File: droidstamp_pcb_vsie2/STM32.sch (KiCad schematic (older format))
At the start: 51 parts, among them P6 CONN_5X2, P8 CONN_12X2, P9 CONN_12X2, Q2 BS170F, Q3 BS170F, Q4 BS170F, Q5 BS170F, Q6 BS170F, Q7 BS170F, Q8 BS170F, Q9 BS170F, U10 STM32F105RC, U11 LT1117CST-3.3, U12 ZXMHC3F381N8, U13 ZXMHC3F381N8, U14 ZXMHC3F381N8, U15 ZXMHC3F381N8, X3 12MHz

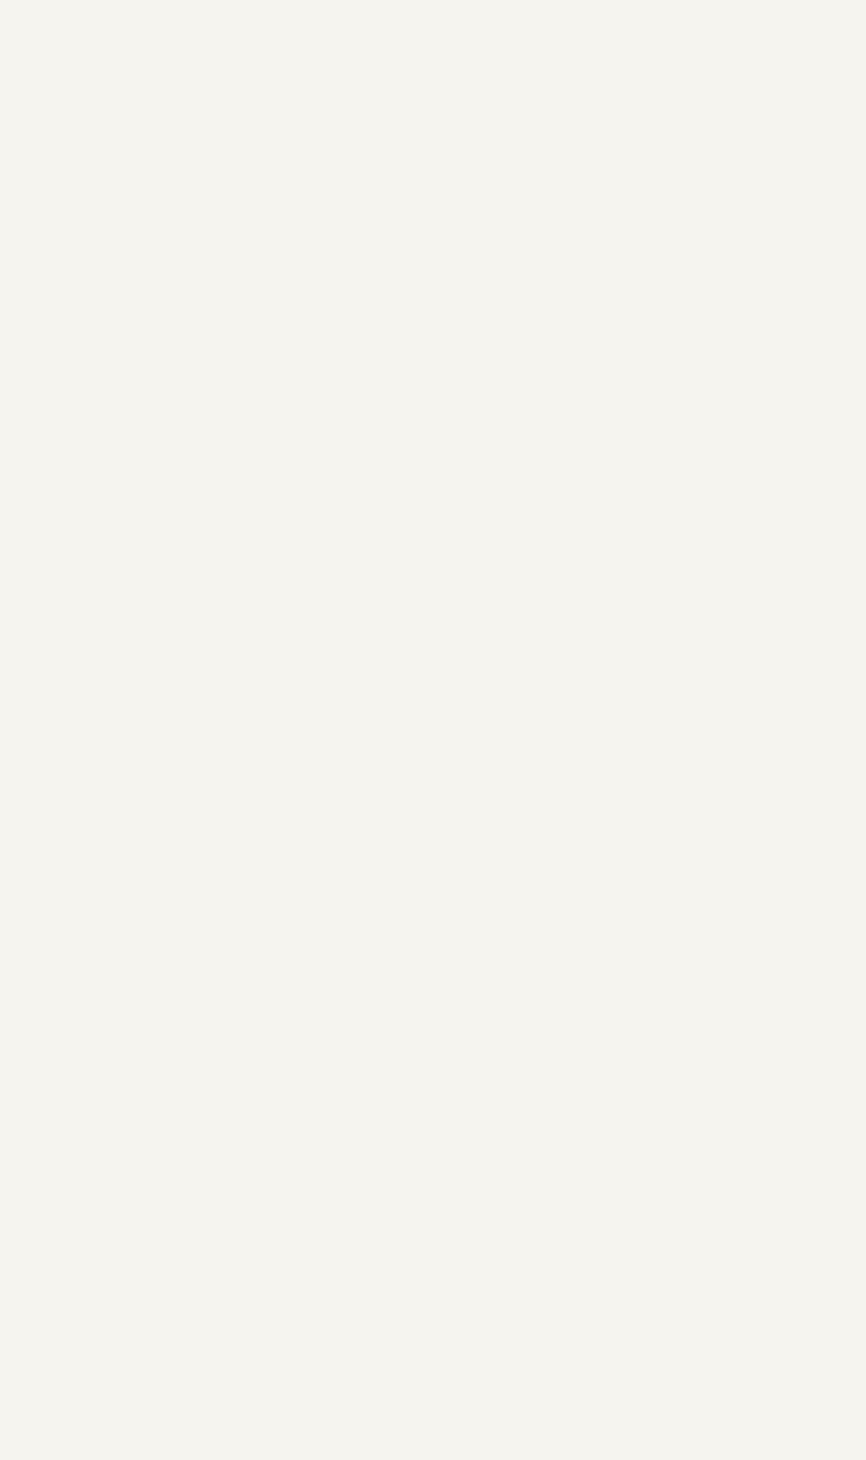
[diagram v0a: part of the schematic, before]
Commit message: se inserto el smt32f4
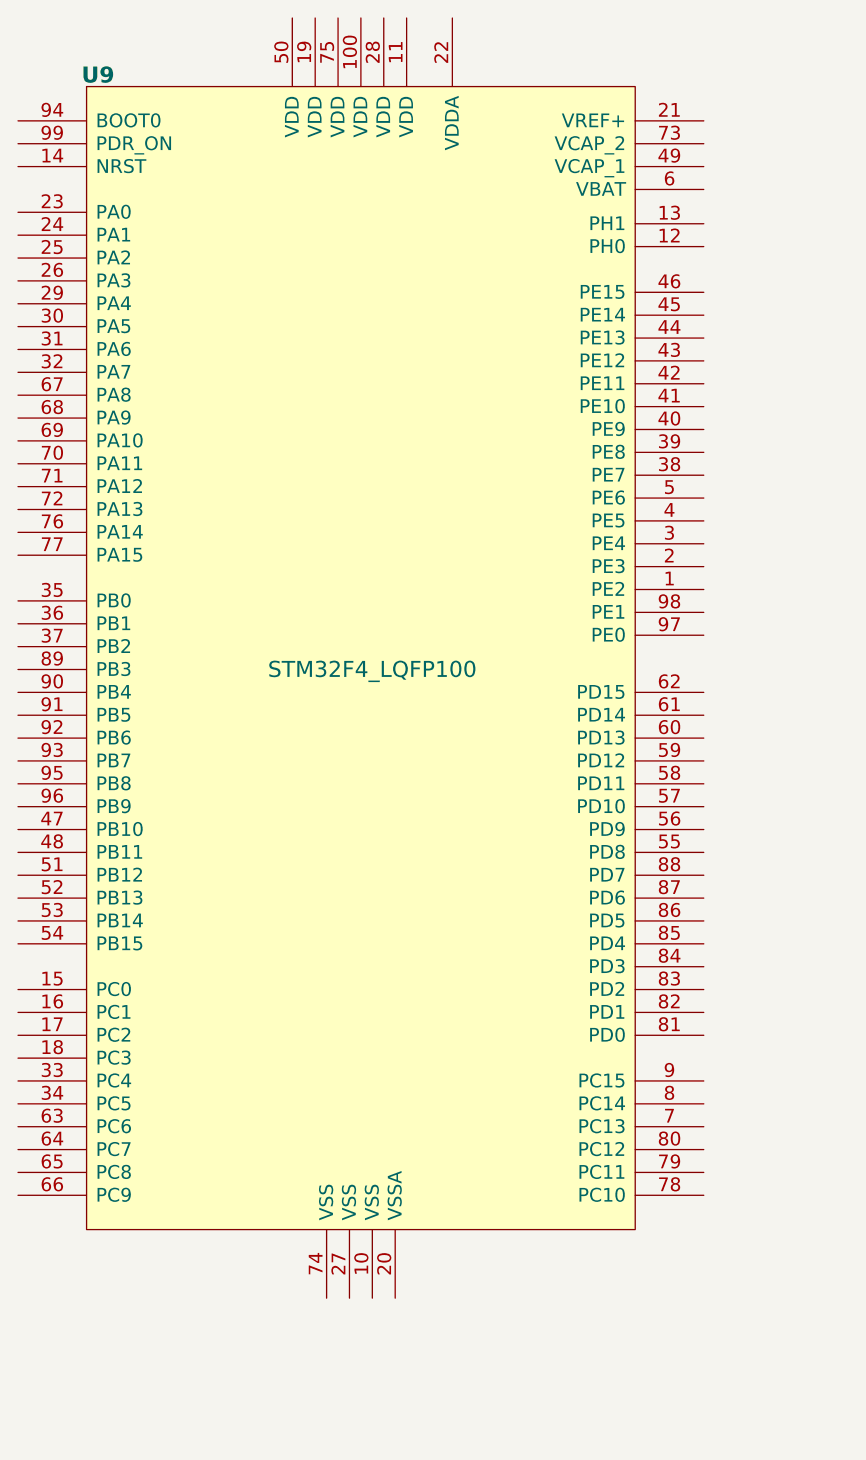
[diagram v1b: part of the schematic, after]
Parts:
- added U9: STM32F4_LQFP100, TQFP_100, symbol STM32F4_LQFP100
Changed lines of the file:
@@
-EESchema Schematic File Version 2  date sáb 03 mar 2012 09:20:54 COT
+EESchema Schematic File Version 2  date Thu 29 Mar 2012 07:34:40 PM COT
 LIBS:con-jack
 LIBS:adm3101e
@@
 LIBS:lt1117cst
 LIBS:zxmhc3f381n8
+LIBS:stm32f4_lqfp100
 LIBS:i.mx233stamp-cache
-EELAYER 24  0
+EELAYER 25  0
 EELAYER END
 $Descr User 12000 10000
-Sheet 3 5
+encoding utf-8
+Sheet 4 5
 Title ""
-Date "3 mar 2012"
+Date "30 mar 2012"
 Rev ""
 Comp ""
@@
 C19, C21 2.2uF para cortex M4\nC19. C21 = Ohms para cortex M3
 $Comp
-L GND #PWR087
+L GND #PWR98
 U 1 1 4F3EDF04
 P 4400 7650
-F 0 "#PWR087" H 4400 7650 30  0001 C CNN
+F 0 "#PWR98" H 4400 7650 30  0001 C CNN
 F 1 "GND" H 4400 7580 30  0001 C CNN
 	1    4400 7650
@@
 $EndComp
 $Comp
-L GND #PWR088
+L GND #PWR97
 U 1 1 4F3EDF01
 P 4200 7650
-F 0 "#PWR088" H 4200 7650 30  0001 C CNN
+F 0 "#PWR97" H 4200 7650 30  0001 C CNN
 F 1 "GND" H 4200 7580 30  0001 C CNN
 	1    4200 7650
@@
 $EndComp
 $Comp
-L 3V3 #PWR95
+L 3V3 #PWR104
 U 1 1 4F3E63FA
 P 6050 8850
-F 0 "#PWR95" H 6050 8950 30  0001 C CNN
+F 0 "#PWR104" H 6050 8950 30  0001 C CNN
 F 1 "3V3" H 6050 8960 30  0000 C CNN
 	1    6050 8850
@@
 $EndComp
 $Comp
-L 3V3 #PWR94
+L 3V3 #PWR103
 U 1 1 4F3E63F9
 P 6050 8750
-F 0 "#PWR94" H 6050 8850 30  0001 C CNN
+F 0 "#PWR103" H 6050 8850 30  0001 C CNN
 F 1 "3V3" H 6050 8860 30  0000 C CNN
 	1    6050 8750
@@
 GND
 $Comp
-L 3V3 #PWR92
+L 3V3 #PWR101
 U 1 1 4F3E4E25
 P 6050 8550
-F 0 "#PWR92" H 6050 8650 30  0001 C CNN
+F 0 "#PWR101" H 6050 8650 30  0001 C CNN
 F 1 "3V3" H 6050 8660 30  0000 C CNN
 	1    6050 8550
@@
 $EndComp
 $Comp
-L 3V3 #PWR93
+L 3V3 #PWR102
 U 1 1 4F3E4E22
 P 6050 8650
-F 0 "#PWR93" H 6050 8750 30  0001 C CNN
+F 0 "#PWR102" H 6050 8750 30  0001 C CNN
 F 1 "3V3" H 6050 8760 30  0000 C CNN
 	1    6050 8650
@@
 $EndComp
 $Comp
-L 3V3 #PWR84
+L 3V3 #PWR93
 U 1 1 4F352D37
 P 2050 6850
-F 0 "#PWR84" H 2050 6950 30  0001 C CNN
+F 0 "#PWR93" H 2050 6950 30  0001 C CNN
 F 1 "3V3" H 2050 6960 30  0000 C CNN
 	1    2050 6850
@@
 I2C1_SDA
 $Comp
-L 3V3 #PWR96
+L 3V3 #PWR105
 U 1 1 4E8A099D
 P 6050 8950
-F 0 "#PWR96" H 6050 9050 30  0001 C CNN
+F 0 "#PWR105" H 6050 9050 30  0001 C CNN
 F 1 "3V3" H 6050 9060 30  0000 C CNN
 	1    6050 8950
@@
 $EndComp
 $Comp
-L 3V3 #PWR85
+L 3V3 #PWR94
 U 1 1 4E8A0997
 P 3700 7900
-F 0 "#PWR85" H 3700 8000 30  0001 C CNN
+F 0 "#PWR94" H 3700 8000 30  0001 C CNN
 F 1 "3V3" H 3700 8010 30  0000 C CNN
 	1    3700 7900
@@
 $EndComp
 $Comp
-L 3V3 #PWR83
+L 3V3 #PWR92
 U 1 1 4E8A0992
 P 1500 7900
-F 0 "#PWR83" H 1500 8000 30  0001 C CNN
+F 0 "#PWR92" H 1500 8000 30  0001 C CNN
 F 1 "3V3" H 1500 8010 30  0000 C CNN
 	1    1500 7900
@@
 $EndComp
 $Comp
-L VDD5V #PWR089
+L VDD5V #PWR106
 U 1 1 4E7B5061
 P 6700 1000
-F 0 "#PWR089" H 6700 1100 30  0001 C CNN
+F 0 "#PWR106" H 6700 1100 30  0001 C CNN
 F 1 "VDD5V" H 6700 1100 30  0000 C CNN
 	1    6700 1000
@@
 $EndComp
 $Comp
-L GND #PWR090
+L GND #PWR107
 U 1 1 4E7B4E89
 P 6700 1650
-F 0 "#PWR090" H 6700 1650 30  0001 C CNN
+F 0 "#PWR107" H 6700 1650 30  0001 C CNN
 F 1 "GND" H 6700 1580 30  0001 C CNN
 	1    6700 1650
@@
 $EndComp
 $Comp
-L GND #PWR091
+L GND #PWR111
 U 1 1 4E7B4E84
 P 8150 1650
-F 0 "#PWR091" H 8150 1650 30  0001 C CNN
+F 0 "#PWR111" H 8150 1650 30  0001 C CNN
 F 1 "GND" H 8150 1580 30  0001 C CNN
 	1    8150 1650
@@
 $EndComp
 $Comp
-L GND #PWR092
+L GND #PWR109
 U 1 1 4E7B44BE
 P 7750 1650
-F 0 "#PWR092" H 7750 1650 30  0001 C CNN
+F 0 "#PWR109" H 7750 1650 30  0001 C CNN
 F 1 "GND" H 7750 1580 30  0001 C CNN
 	1    7750 1650
@@
 $EndComp
 $Comp
-L GND #PWR093
+L GND #PWR108
 U 1 1 4E7B44A2
 P 6900 1250
-F 0 "#PWR093" H 6900 1250 30  0001 C CNN
+F 0 "#PWR108" H 6900 1250 30  0001 C CNN
 F 1 "GND" H 6900 1180 30  0001 C CNN
 	1    6900 1250
@@
 $EndComp
 $Comp
-L 3V3 #PWR101
+L 3V3 #PWR110
 U 1 1 4E7B4482
 P 8150 900
-F 0 "#PWR101" H 8150 1000 30  0001 C CNN
+F 0 "#PWR110" H 8150 1000 30  0001 C CNN
 F 1 "3V3" H 8150 1010 30  0000 C CNN
 	1    8150 900
@@
 $EndComp
 $Comp
-L GND #PWR094
+L GND #PWR120
 U 1 1 4E78C5F4
 P 10800 2850
-F 0 "#PWR094" H 10800 2850 30  0001 C CNN
+F 0 "#PWR120" H 10800 2850 30  0001 C CNN
 F 1 "GND" H 10800 2780 30  0001 C CNN
 	1    10800 2850
@@
 $EndComp
 $Comp
-L 3V3 #PWR104
+L 3V3 #PWR113
 U 1 1 4E78C319
 P 8550 2150
-F 0 "#PWR104" H 8550 2250 30  0001 C CNN
+F 0 "#PWR113" H 8550 2250 30  0001 C CNN
 F 1 "3V3" H 8550 2260 30  0000 C CNN
 	1    8550 2150
@@
 $EndComp
 $Comp
-L GND #PWR095
+L GND #PWR100
 U 1 1 4E78C2ED
 P 5300 7400
-F 0 "#PWR095" H 5300 7400 30  0001 C CNN
+F 0 "#PWR100" H 5300 7400 30  0001 C CNN
 F 1 "GND" H 5300 7330 30  0001 C CNN
 	1    5300 7400
@@
 JTDI
 $Comp
-L 3V3 #PWR87
+L 3V3 #PWR96
 U 1 1 4E78BA06
 P 4150 1100
-F 0 "#PWR87" H 4150 1200 30  0001 C CNN
+F 0 "#PWR96" H 4150 1200 30  0001 C CNN
 F 1 "3V3" H 4150 1210 30  0000 C CNN
 	1    4150 1100
@@
 $EndComp
 $Comp
-L 3V3 #PWR103
+L 3V3 #PWR112
 U 1 1 4E2A2E11
 P 8350 2150
-F 0 "#PWR103" H 8350 2250 30  0001 C CNN
+F 0 "#PWR112" H 8350 2250 30  0001 C CNN
 F 1 "3V3" H 8350 2260 30  0000 C CNN
 	1    8350 2150
@@
 $EndComp
 $Comp
-L 3V3 #PWR106
+L 3V3 #PWR115
 U 1 1 4E2A2E03
 P 8750 1000
-F 0 "#PWR106" H 8750 1100 30  0001 C CNN
+F 0 "#PWR115" H 8750 1100 30  0001 C CNN
 F 1 "3V3" H 8750 1110 30  0000 C CNN
 	1    8750 1000
@@
 $EndComp
 $Comp
-L 3V3 #PWR90
+L 3V3 #PWR99
 U 1 1 4E2A2DF0
 P 4700 1150
-F 0 "#PWR90" H 4700 1250 30  0001 C CNN
+F 0 "#PWR99" H 4700 1250 30  0001 C CNN
 F 1 "3V3" H 4700 1260 30  0000 C CNN
 	1    4700 1150
@@
 $EndComp
 $Comp
-L GND #PWR096
+L GND #PWR119
 U 1 1 4E188E4E
 P 10550 1500
-F 0 "#PWR096" H 10550 1500 30  0001 C CNN
+F 0 "#PWR119" H 10550 1500 30  0001 C CNN
 F 1 "GND" H 10550 1430 30  0001 C CNN
 	1    10550 1500
@@
 FP1
 $Comp
-L GND #PWR097
+L GND #PWR116
 U 1 1 4E186DEB
 P 9250 1500
-F 0 "#PWR097" H 9250 1500 30  0001 C CNN
+F 0 "#PWR116" H 9250 1500 30  0001 C CNN
 F 1 "GND" H 9250 1430 30  0001 C CNN
 	1    9250 1500
@@
 $EndComp
 $Comp
-L GND #PWR098
+L GND #PWR114
 U 1 1 4E07869F
 P 8550 2800
-F 0 "#PWR098" H 8550 2800 30  0001 C CNN
+F 0 "#PWR114" H 8550 2800 30  0001 C CNN
 F 1 "GND" H 8550 2730 30  0001 C CNN
 	1    8550 2800
@@
 $EndComp
 $Comp
-L GND #PWR099
+L GND #PWR95
 U 1 1 4DCDB18D
 P 4000 7400
-F 0 "#PWR099" H 4000 7400 30  0001 C CNN
+F 0 "#PWR95" H 4000 7400 30  0001 C CNN
 F 1 "GND" H 4000 7330 30  0001 C CNN
 	1    4000 7400
@@
 $EndComp
 $Comp
-L GND #PWR0100
+L GND #PWR117
 U 1 1 4DCDB183
 P 9650 2800
-F 0 "#PWR0100" H 9650 2800 30  0001 C CNN
+F 0 "#PWR117" H 9650 2800 30  0001 C CNN
 F 1 "GND" H 9650 2730 30  0001 C CNN
 	1    9650 2800
@@
 NRST
 $Comp
-L GND #PWR0101
+L GND #PWR91
 U 1 1 4DCDB180
 P 700 2050
-F 0 "#PWR0101" H 700 2050 30  0001 C CNN
+F 0 "#PWR91" H 700 2050 30  0001 C CNN
 F 1 "GND" H 700 1980 30  0001 C CNN
 	1    700  2050
@@
 BOOT0
 $Comp
-L GND #PWR0102
+L GND #PWR118
 U 1 1 4DCDB17D
 P 10400 2850
-F 0 "#PWR0102" H 10400 2850 30  0001 C CNN
+F 0 "#PWR118" H 10400 2850 30  0001 C CNN
 F 1 "GND" H 10400 2780 30  0001 C CNN
 	1    10400 2850
@@
 	0    1    1    0
 $EndComp
+$Comp
+L STM32F4_LQFP100 U9
+U 1 1 4F750C24
+P -2750 950
+F 0 "U9" H -4000 3350 70  0000 C CNB
+F 1 "STM32F4_LQFP100" H -2800 750 70  0000 C CNN
+F 2 "TQFP_100" H -2750 950 60  0001 C CNN
+	1    -2750 950
+	1    0    0    -1
+$EndComp
 $EndSCHEMATC

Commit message: sync with las sie_bot_v2
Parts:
- removed U9: STM32F4_LQFP100, TQFP_100, symbol STM32F4_LQFP100
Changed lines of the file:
@@
-EESchema Schematic File Version 2  date Thu 29 Mar 2012 07:34:40 PM COT
+EESchema Schematic File Version 2  date Fri 30 Mar 2012 08:38:46 AM COT
 LIBS:con-jack
 LIBS:adm3101e
@@
 LIBS:lt1117cst
 LIBS:zxmhc3f381n8
-LIBS:stm32f4_lqfp100
 LIBS:i.mx233stamp-cache
 EELAYER 25  0
@@
 $Descr User 12000 10000
 encoding utf-8
-Sheet 4 5
+Sheet 3 5
 Title ""
 Date "30 mar 2012"
@@
 C19, C21 2.2uF para cortex M4\nC19. C21 = Ohms para cortex M3
 $Comp
-L GND #PWR98
+L GND #PWR087
 U 1 1 4F3EDF04
 P 4400 7650
-F 0 "#PWR98" H 4400 7650 30  0001 C CNN
+F 0 "#PWR087" H 4400 7650 30  0001 C CNN
 F 1 "GND" H 4400 7580 30  0001 C CNN
 	1    4400 7650
@@
 $EndComp
 $Comp
-L GND #PWR97
+L GND #PWR088
 U 1 1 4F3EDF01
 P 4200 7650
-F 0 "#PWR97" H 4200 7650 30  0001 C CNN
+F 0 "#PWR088" H 4200 7650 30  0001 C CNN
 F 1 "GND" H 4200 7580 30  0001 C CNN
 	1    4200 7650
@@
 $EndComp
 $Comp
-L 3V3 #PWR104
+L 3V3 #PWR95
 U 1 1 4F3E63FA
 P 6050 8850
-F 0 "#PWR104" H 6050 8950 30  0001 C CNN
+F 0 "#PWR95" H 6050 8950 30  0001 C CNN
 F 1 "3V3" H 6050 8960 30  0000 C CNN
 	1    6050 8850
@@
 $EndComp
 $Comp
-L 3V3 #PWR103
+L 3V3 #PWR94
 U 1 1 4F3E63F9
 P 6050 8750
-F 0 "#PWR103" H 6050 8850 30  0001 C CNN
+F 0 "#PWR94" H 6050 8850 30  0001 C CNN
 F 1 "3V3" H 6050 8860 30  0000 C CNN
 	1    6050 8750
@@
 GND
 $Comp
-L 3V3 #PWR101
+L 3V3 #PWR92
 U 1 1 4F3E4E25
 P 6050 8550
-F 0 "#PWR101" H 6050 8650 30  0001 C CNN
+F 0 "#PWR92" H 6050 8650 30  0001 C CNN
 F 1 "3V3" H 6050 8660 30  0000 C CNN
 	1    6050 8550
@@
 $EndComp
 $Comp
-L 3V3 #PWR102
+L 3V3 #PWR93
 U 1 1 4F3E4E22
 P 6050 8650
-F 0 "#PWR102" H 6050 8750 30  0001 C CNN
+F 0 "#PWR93" H 6050 8750 30  0001 C CNN
 F 1 "3V3" H 6050 8760 30  0000 C CNN
 	1    6050 8650
@@
 $EndComp
 $Comp
-L 3V3 #PWR93
+L 3V3 #PWR84
 U 1 1 4F352D37
 P 2050 6850
-F 0 "#PWR93" H 2050 6950 30  0001 C CNN
+F 0 "#PWR84" H 2050 6950 30  0001 C CNN
 F 1 "3V3" H 2050 6960 30  0000 C CNN
 	1    2050 6850
@@
 I2C1_SDA
 $Comp
-L 3V3 #PWR105
+L 3V3 #PWR96
 U 1 1 4E8A099D
 P 6050 8950
-F 0 "#PWR105" H 6050 9050 30  0001 C CNN
+F 0 "#PWR96" H 6050 9050 30  0001 C CNN
 F 1 "3V3" H 6050 9060 30  0000 C CNN
 	1    6050 8950
@@
 $EndComp
 $Comp
-L 3V3 #PWR94
+L 3V3 #PWR85
 U 1 1 4E8A0997
 P 3700 7900
-F 0 "#PWR94" H 3700 8000 30  0001 C CNN
+F 0 "#PWR85" H 3700 8000 30  0001 C CNN
 F 1 "3V3" H 3700 8010 30  0000 C CNN
 	1    3700 7900
@@
 $EndComp
 $Comp
-L 3V3 #PWR92
+L 3V3 #PWR83
 U 1 1 4E8A0992
 P 1500 7900
-F 0 "#PWR92" H 1500 8000 30  0001 C CNN
+F 0 "#PWR83" H 1500 8000 30  0001 C CNN
 F 1 "3V3" H 1500 8010 30  0000 C CNN
 	1    1500 7900
@@
 $EndComp
 $Comp
-L VDD5V #PWR106
+L VDD5V #PWR089
 U 1 1 4E7B5061
 P 6700 1000
-F 0 "#PWR106" H 6700 1100 30  0001 C CNN
+F 0 "#PWR089" H 6700 1100 30  0001 C CNN
 F 1 "VDD5V" H 6700 1100 30  0000 C CNN
 	1    6700 1000
@@
 $EndComp
 $Comp
-L GND #PWR107
+L GND #PWR090
 U 1 1 4E7B4E89
 P 6700 1650
-F 0 "#PWR107" H 6700 1650 30  0001 C CNN
+F 0 "#PWR090" H 6700 1650 30  0001 C CNN
 F 1 "GND" H 6700 1580 30  0001 C CNN
 	1    6700 1650
@@
 $EndComp
 $Comp
-L GND #PWR111
+L GND #PWR091
 U 1 1 4E7B4E84
 P 8150 1650
-F 0 "#PWR111" H 8150 1650 30  0001 C CNN
+F 0 "#PWR091" H 8150 1650 30  0001 C CNN
 F 1 "GND" H 8150 1580 30  0001 C CNN
 	1    8150 1650
@@
 $EndComp
 $Comp
-L GND #PWR109
+L GND #PWR092
 U 1 1 4E7B44BE
 P 7750 1650
-F 0 "#PWR109" H 7750 1650 30  0001 C CNN
+F 0 "#PWR092" H 7750 1650 30  0001 C CNN
 F 1 "GND" H 7750 1580 30  0001 C CNN
 	1    7750 1650
@@
 $EndComp
 $Comp
-L GND #PWR108
+L GND #PWR093
 U 1 1 4E7B44A2
 P 6900 1250
-F 0 "#PWR108" H 6900 1250 30  0001 C CNN
+F 0 "#PWR093" H 6900 1250 30  0001 C CNN
 F 1 "GND" H 6900 1180 30  0001 C CNN
 	1    6900 1250
@@
 $EndComp
 $Comp
-L 3V3 #PWR110
+L 3V3 #PWR101
 U 1 1 4E7B4482
 P 8150 900
-F 0 "#PWR110" H 8150 1000 30  0001 C CNN
+F 0 "#PWR101" H 8150 1000 30  0001 C CNN
 F 1 "3V3" H 8150 1010 30  0000 C CNN
 	1    8150 900
@@
 $EndComp
 $Comp
-L GND #PWR120
+L GND #PWR094
 U 1 1 4E78C5F4
 P 10800 2850
-F 0 "#PWR120" H 10800 2850 30  0001 C CNN
+F 0 "#PWR094" H 10800 2850 30  0001 C CNN
 F 1 "GND" H 10800 2780 30  0001 C CNN
 	1    10800 2850
@@
 $EndComp
 $Comp
-L 3V3 #PWR113
+L 3V3 #PWR104
 U 1 1 4E78C319
 P 8550 2150
-F 0 "#PWR113" H 8550 2250 30  0001 C CNN
+F 0 "#PWR104" H 8550 2250 30  0001 C CNN
 F 1 "3V3" H 8550 2260 30  0000 C CNN
 	1    8550 2150
@@
 $EndComp
 $Comp
-L GND #PWR100
+L GND #PWR095
 U 1 1 4E78C2ED
 P 5300 7400
-F 0 "#PWR100" H 5300 7400 30  0001 C CNN
+F 0 "#PWR095" H 5300 7400 30  0001 C CNN
 F 1 "GND" H 5300 7330 30  0001 C CNN
 	1    5300 7400
@@
 JTDI
 $Comp
-L 3V3 #PWR96
+L 3V3 #PWR87
 U 1 1 4E78BA06
 P 4150 1100
-F 0 "#PWR96" H 4150 1200 30  0001 C CNN
+F 0 "#PWR87" H 4150 1200 30  0001 C CNN
 F 1 "3V3" H 4150 1210 30  0000 C CNN
 	1    4150 1100
@@
 $EndComp
 $Comp
-L 3V3 #PWR112
+L 3V3 #PWR103
 U 1 1 4E2A2E11
 P 8350 2150
-F 0 "#PWR112" H 8350 2250 30  0001 C CNN
+F 0 "#PWR103" H 8350 2250 30  0001 C CNN
 F 1 "3V3" H 8350 2260 30  0000 C CNN
 	1    8350 2150
@@
 $EndComp
 $Comp
-L 3V3 #PWR115
+L 3V3 #PWR106
 U 1 1 4E2A2E03
 P 8750 1000
-F 0 "#PWR115" H 8750 1100 30  0001 C CNN
+F 0 "#PWR106" H 8750 1100 30  0001 C CNN
 F 1 "3V3" H 8750 1110 30  0000 C CNN
 	1    8750 1000
@@
 $EndComp
 $Comp
-L 3V3 #PWR99
+L 3V3 #PWR90
 U 1 1 4E2A2DF0
 P 4700 1150
-F 0 "#PWR99" H 4700 1250 30  0001 C CNN
+F 0 "#PWR90" H 4700 1250 30  0001 C CNN
 F 1 "3V3" H 4700 1260 30  0000 C CNN
 	1    4700 1150
@@
 $EndComp
 $Comp
-L GND #PWR119
+L GND #PWR096
 U 1 1 4E188E4E
 P 10550 1500
-F 0 "#PWR119" H 10550 1500 30  0001 C CNN
+F 0 "#PWR096" H 10550 1500 30  0001 C CNN
 F 1 "GND" H 10550 1430 30  0001 C CNN
 	1    10550 1500
@@
 FP1
 $Comp
-L GND #PWR116
+L GND #PWR097
 U 1 1 4E186DEB
 P 9250 1500
-F 0 "#PWR116" H 9250 1500 30  0001 C CNN
+F 0 "#PWR097" H 9250 1500 30  0001 C CNN
 F 1 "GND" H 9250 1430 30  0001 C CNN
 	1    9250 1500
@@
 $EndComp
 $Comp
-L GND #PWR114
+L GND #PWR098
 U 1 1 4E07869F
 P 8550 2800
-F 0 "#PWR114" H 8550 2800 30  0001 C CNN
+F 0 "#PWR098" H 8550 2800 30  0001 C CNN
 F 1 "GND" H 8550 2730 30  0001 C CNN
 	1    8550 2800
@@
 $EndComp
 $Comp
-L GND #PWR95
+L GND #PWR099
 U 1 1 4DCDB18D
 P 4000 7400
-F 0 "#PWR95" H 4000 7400 30  0001 C CNN
+F 0 "#PWR099" H 4000 7400 30  0001 C CNN
 F 1 "GND" H 4000 7330 30  0001 C CNN
 	1    4000 7400
@@
 $EndComp
 $Comp
-L GND #PWR117
+L GND #PWR0100
 U 1 1 4DCDB183
 P 9650 2800
-F 0 "#PWR117" H 9650 2800 30  0001 C CNN
+F 0 "#PWR0100" H 9650 2800 30  0001 C CNN
 F 1 "GND" H 9650 2730 30  0001 C CNN
 	1    9650 2800
@@
 NRST
 $Comp
-L GND #PWR91
+L GND #PWR0101
 U 1 1 4DCDB180
 P 700 2050
-F 0 "#PWR91" H 700 2050 30  0001 C CNN
+F 0 "#PWR0101" H 700 2050 30  0001 C CNN
 F 1 "GND" H 700 1980 30  0001 C CNN
 	1    700  2050
@@
 BOOT0
 $Comp
-L GND #PWR118
+L GND #PWR0102
 U 1 1 4DCDB17D
 P 10400 2850
-F 0 "#PWR118" H 10400 2850 30  0001 C CNN
+F 0 "#PWR0102" H 10400 2850 30  0001 C CNN
 F 1 "GND" H 10400 2780 30  0001 C CNN
 	1    10400 2850
@@
 	0    1    1    0
 $EndComp
-$Comp
-L STM32F4_LQFP100 U9
-U 1 1 4F750C24
-P -2750 950
-F 0 "U9" H -4000 3350 70  0000 C CNB
-F 1 "STM32F4_LQFP100" H -2800 750 70  0000 C CNN
-F 2 "TQFP_100" H -2750 950 60  0001 C CNN
-	1    -2750 950
-	1    0    0    -1
-$EndComp
 $EndSCHEMATC

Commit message: se inserto el smt32f4
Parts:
- added U9: STM32F4_LQFP100, TQFP_100, symbol STM32F4_LQFP100
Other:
- moved on the sheet: C19, C21, L14, R46

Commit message: mas conexiones al stm32f4
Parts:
- removed U10: STM32F105RC, TQFP_64, symbol STM32F105RC
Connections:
- wire segments 252 -> 257
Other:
- moved on the sheet: C26, C28, X3
